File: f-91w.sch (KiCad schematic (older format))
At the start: 19 parts, among them P10 CONN_01X01, P11 CONN_01X01, P13 CONN_01X01, P14 CONN_01X01, P5 CONN_01X01, P6 CONN_01X01, P7 CONN_01X01, P8 CONN_01X01, P9 CONN_01X01, Q1 BC846, U2 LCD-F-91W, U3 TSOP57xxx, U4 MAG3110

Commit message: Add PSoC 4, decoupling and crystals
No connection to rest of system yet
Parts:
- added AE?: TBD, symbol Antenna_Shield
- added C?: 24pF, symbol C_Small
- added C?: 47pF, symbol C_Small
- added C? (x2): C_Small, symbol C_Small
- added C?: 1uF, symbol C_Small
- added L?: L_Small, symbol L_Small
- added U?: CY8C4248LQI-BL483, symbol CY8C4248LQI-BL483
- added Y?: 32.768KHz, symbol Crystal_Small
- added Y?: 24MHz, symbol Crystal_GND24
- P10, P11, P13, P14, P5, P6, P7, P8, P9: symbol CONN_01X01 -> Conn_01x01
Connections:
- net labels added: /XRES, SWCLK, SWDIO, VDDA, VDDD, VDDR
- wire segments 74 -> 122
- no-connect marks 0 -> 1

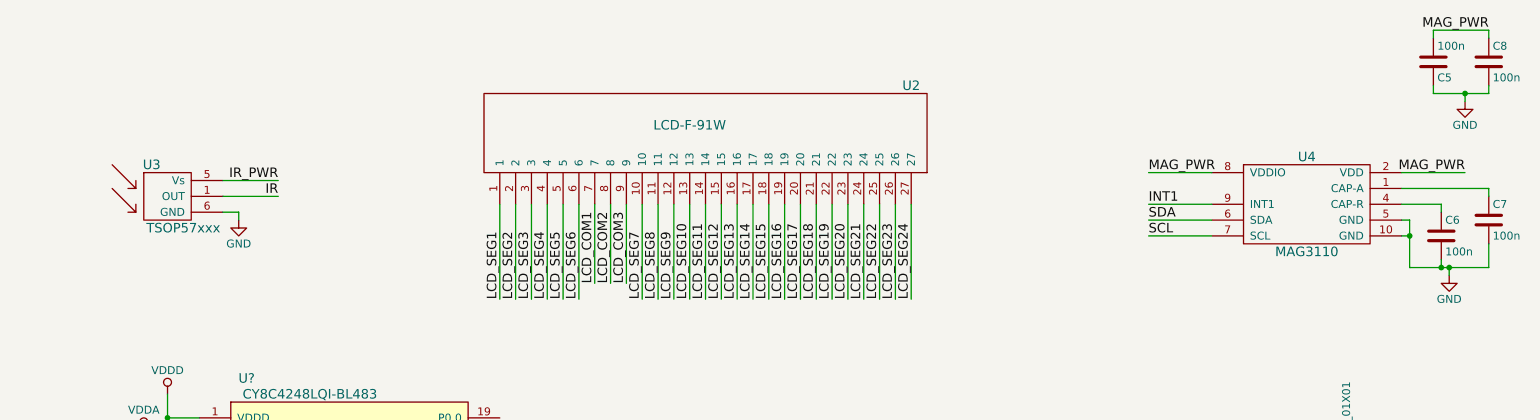
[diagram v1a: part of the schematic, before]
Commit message: Delete magnetometer and IR reciever
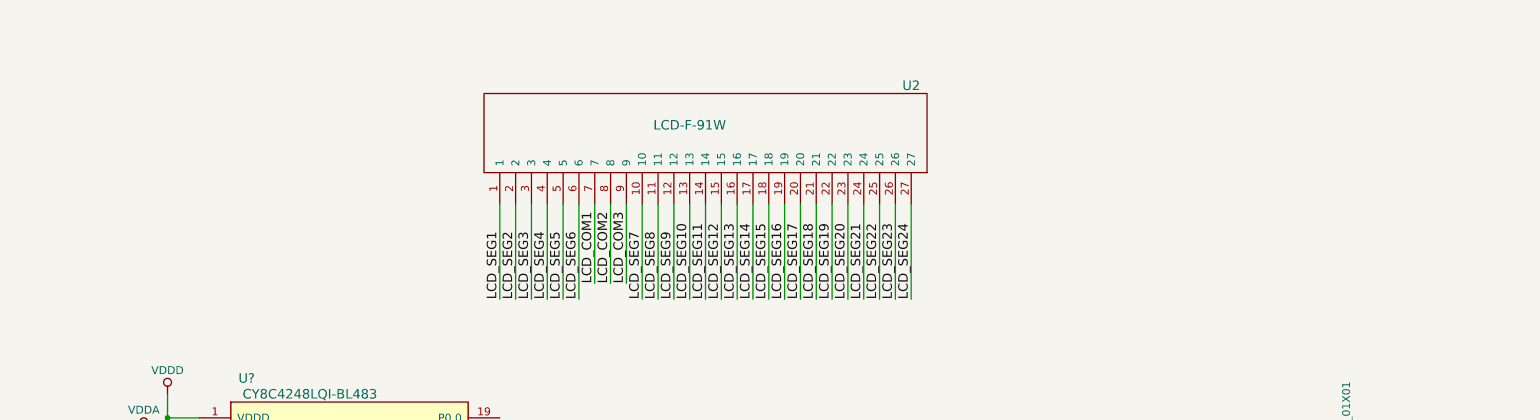
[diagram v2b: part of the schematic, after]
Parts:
- removed C5, C6, C7, C8: 100n, Capacitors_SMD:C_0402, symbol C
- removed U3: TSOP57xxx, f-91w:TSOP57xxx, symbol TSOP57xxx
- removed U4: MAG3110, Housings_DFN_QFN:DFN-10-1EP_2x2mm_Pitch0.4mm, symbol MAG3110
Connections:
- net labels removed: INT1, IR, IR_PWR, MAG_PWR, SCL, SDA
- wire segments 122 -> 95
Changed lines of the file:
@@
 $EndComp
-$Comp
-L TSOP57xxx U3
-U 1 1 56F47D47
-P 2350 1800
-F 0 "U3" H 2250 2000 60  0000 C CNN
-F 1 "TSOP57xxx" H 2450 1600 60  0000 C CNN
-F 2 "f-91w:TSOP57xxx" H 2350 1800 60  0001 C CNN
-F 3 "" H 2350 1800 60  0000 C CNN
-	1    2350 1800
-	1    0    0    -1
-$EndComp
-$Comp
-L GND #PWR02
-U 1 1 56F47FA1
-P 2800 1950
-F 0 "#PWR02" H 2800 1700 50  0001 C CNN
-F 1 "GND" H 2800 1800 50  0000 C CNN
-F 2 "" H 2800 1950 50  0000 C CNN
-F 3 "" H 2800 1950 50  0000 C CNN
-	1    2800 1950
-	1    0    0    -1
-$EndComp
-Text Label 3050 1700 2    60   ~ 0
-IR_PWR
-Text Label 3050 1800 2    60   ~ 0
-IR
 $Comp
 L R R3
@@
 	1    0    0    -1
 $EndComp
-$Comp
-L C C5
-U 1 1 5700E1C2
-P 10350 950
-F 0 "C5" H 10375 1050 50  0000 L CNN
-F 1 "100n" H 10375 850 50  0000 L CNN
-F 2 "Capacitors_SMD:C_0402" H 10388 800 50  0001 C CNN
-F 3 "" H 10350 950 50  0000 C CNN
-	1    10350 950
-	1    0    0    1
-$EndComp
-$Comp
-L GND #PWR06
-U 1 1 5700F75E
-P 10550 1200
-F 0 "#PWR06" H 10550 950 50  0001 C CNN
-F 1 "GND" H 10550 1050 50  0000 C CNN
-F 2 "" H 10550 1200 50  0000 C CNN
-F 3 "" H 10550 1200 50  0000 C CNN
-	1    10550 1200
-	1    0    0    -1
-$EndComp
-$Comp
-L GND #PWR07
-U 1 1 5700F854
-P 10450 2300
-F 0 "#PWR07" H 10450 2050 50  0001 C CNN
-F 1 "GND" H 10450 2150 50  0000 C CNN
-F 2 "" H 10450 2300 50  0000 C CNN
-F 3 "" H 10450 2300 50  0000 C CNN
-	1    10450 2300
-	1    0    0    -1
-$EndComp
-$Comp
-L C C6
-U 1 1 5700FED8
-P 10400 2050
-F 0 "C6" H 10425 2150 50  0000 L CNN
-F 1 "100n" H 10425 1950 50  0000 L CNN
-F 2 "Capacitors_SMD:C_0402" H 10438 1900 50  0001 C CNN
-F 3 "" H 10400 2050 50  0000 C CNN
-	1    10400 2050
-	1    0    0    -1
-$EndComp
-$Comp
-L C C7
-U 1 1 5700FF6D
-P 10700 1950
-F 0 "C7" H 10725 2050 50  0000 L CNN
-F 1 "100n" H 10725 1850 50  0000 L CNN
-F 2 "Capacitors_SMD:C_0402" H 10738 1800 50  0001 C CNN
-F 3 "" H 10700 1950 50  0000 C CNN
-	1    10700 1950
-	1    0    0    -1
-$EndComp
-Text Label 8550 1850 0    60   ~ 0
-INT1
-Text Label 8550 1950 0    60   ~ 0
-SDA
-Text Label 8550 2050 0    60   ~ 0
-SCL
-$Comp
-L MAG3110 U4
-U 1 1 57006D5B
-P 9550 1900
-F 0 "U4" H 9550 2250 60  0000 C CNN
-F 1 "MAG3110" H 9550 1650 60  0000 C CNN
-F 2 "Housings_DFN_QFN:DFN-10-1EP_2x2mm_Pitch0.4mm" H 9550 1900 60  0001 C CNN
-F 3 "" H 9550 1900 60  0000 C CNN
-	1    9550 1900
-	1    0    0    -1
-$EndComp
 Text Label 10100 3800 2    60   ~ 0
 BUZ
-$Comp
-L C C8
-U 1 1 57057DE2
-P 10700 950
-F 0 "C8" H 10725 1050 50  0000 L CNN
-F 1 "100n" H 10725 850 50  0000 L CNN
-F 2 "Capacitors_SMD:C_0402" H 10738 800 50  0001 C CNN
-F 3 "" H 10700 950 50  0000 C CNN
-	1    10700 950
-	1    0    0    -1
-$EndComp
 Text Label 8400 4350 2    60   ~ 0
 B_ALARM
@@
 Text Label 9400 4950 2    60   ~ 0
 LED_2
-Text Label 8550 1650 0    60   ~ 0
-MAG_PWR
-Text Label 10700 750  2    60   ~ 0
-MAG_PWR
-Text Label 10550 1650 2    60   ~ 0
-MAG_PWR
 $Comp
 L GND #PWR08
@@
 	8800 4050 9150 4050
 Wire Wire Line
-	2700 1700 3050 1700
-Wire Wire Line
-	2800 1950 2800 1900
-Wire Wire Line
-	2800 1900 2700 1900
-Wire Wire Line
-	2700 1800 3050 1800
-Wire Wire Line
 	10050 4700 9800 4700
 Wire Wire Line
 	7000 5050 7000 4900
 Wire Wire Line
-	8950 1650 8550 1650
-Wire Wire Line
 	6550 4600 6600 4600
 Wire Wire Line
@@
 	9400 4950 9750 4950
 Wire Wire Line
-	10350 1150 10350 1100
-Wire Wire Line
-	10150 1950 10200 1950
-Wire Wire Line
-	10200 1950 10200 2250
-Wire Wire Line
-	10150 2050 10200 2050
-Connection ~ 10200 2050
-Wire Wire Line
-	10150 1750 10700 1750
-Wire Wire Line
-	10700 1750 10700 1800
-Wire Wire Line
-	10150 1850 10400 1850
-Wire Wire Line
-	10400 1850 10400 1900
-Wire Wire Line
-	10200 2250 10700 2250
-Wire Wire Line
-	10700 2250 10700 2100
-Wire Wire Line
-	10400 2200 10400 2250
-Connection ~ 10400 2250
-Wire Wire Line
-	10450 2250 10450 2300
-Connection ~ 10450 2250
-Wire Wire Line
-	8550 1950 8950 1950
-Wire Wire Line
-	8550 2050 8950 2050
-Wire Wire Line
-	8950 1850 8550 1850
-Wire Wire Line
 	7950 4350 8600 4350
-Wire Wire Line
-	10350 800  10350 750
-Wire Wire Line
-	10150 1650 10550 1650
 Wire Wire Line
 	6550 4550 6550 4600
@@
 Connection ~ 9800 3800
 Wire Wire Line
-	10700 750  10700 800
-Wire Wire Line
-	10350 1150 10700 1150
-Wire Wire Line
-	10700 1150 10700 1100
-Wire Wire Line
-	10550 1200 10550 1150
-Connection ~ 10550 1150
-Wire Wire Line
-	10350 750  10700 750
-Wire Wire Line
 	2550 6950 2450 6950

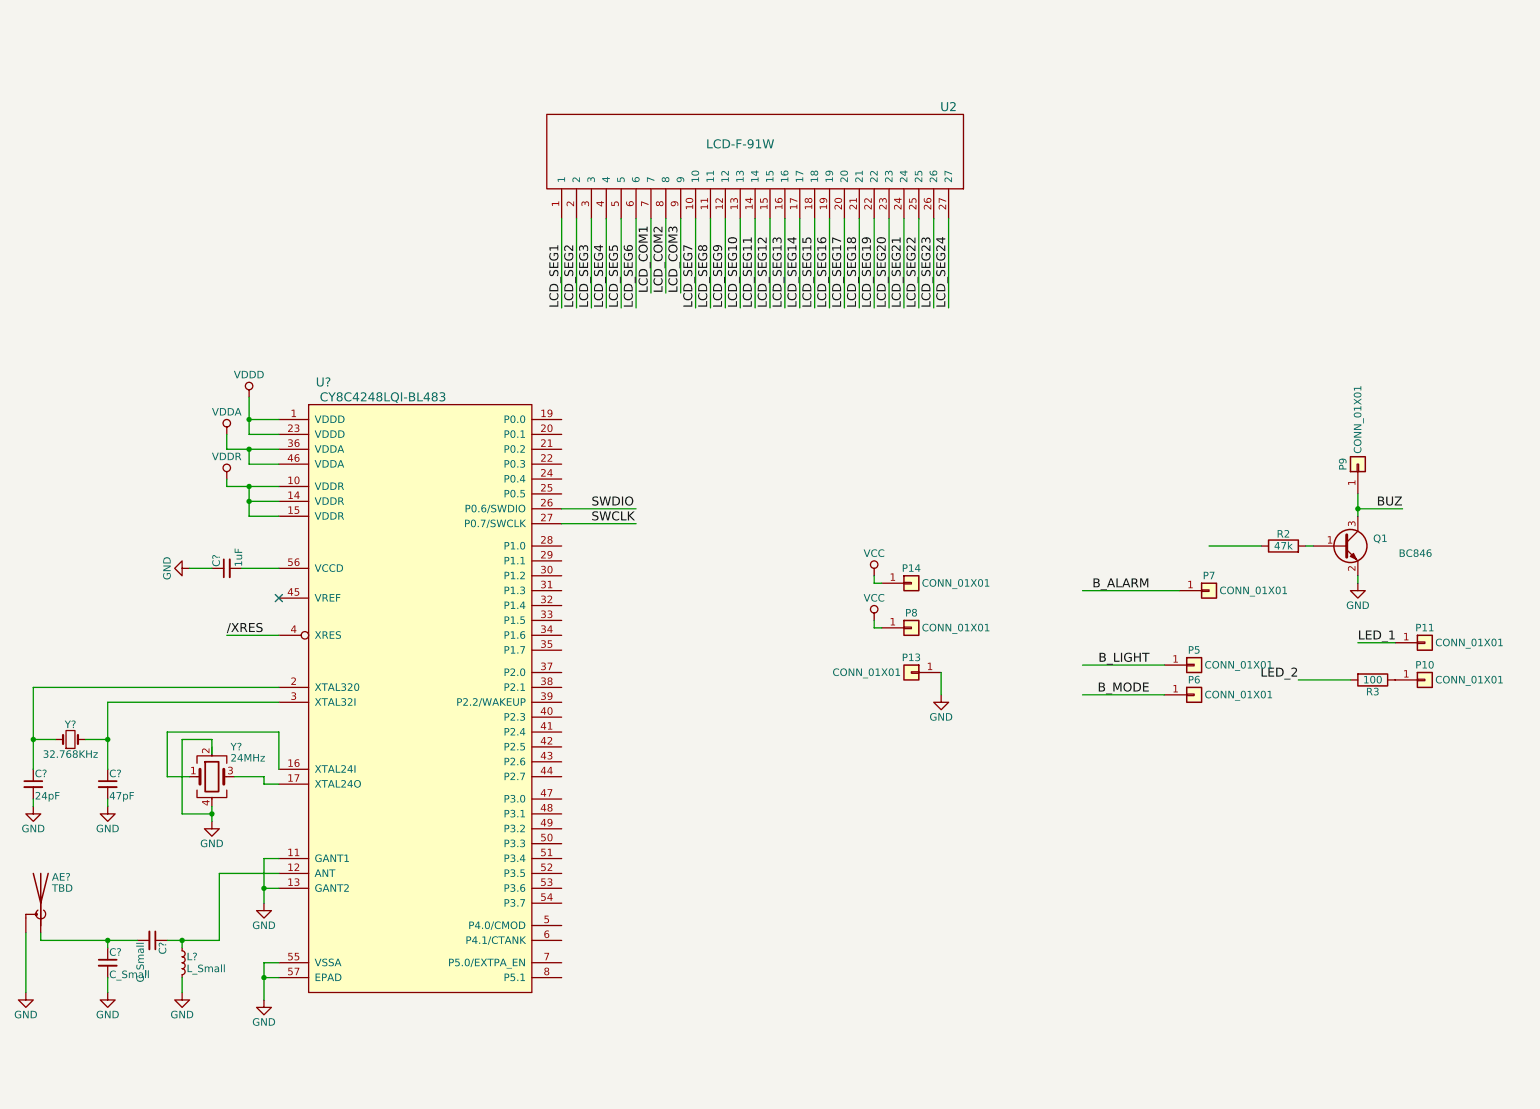
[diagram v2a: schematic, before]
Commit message: Add BME680 to schematic
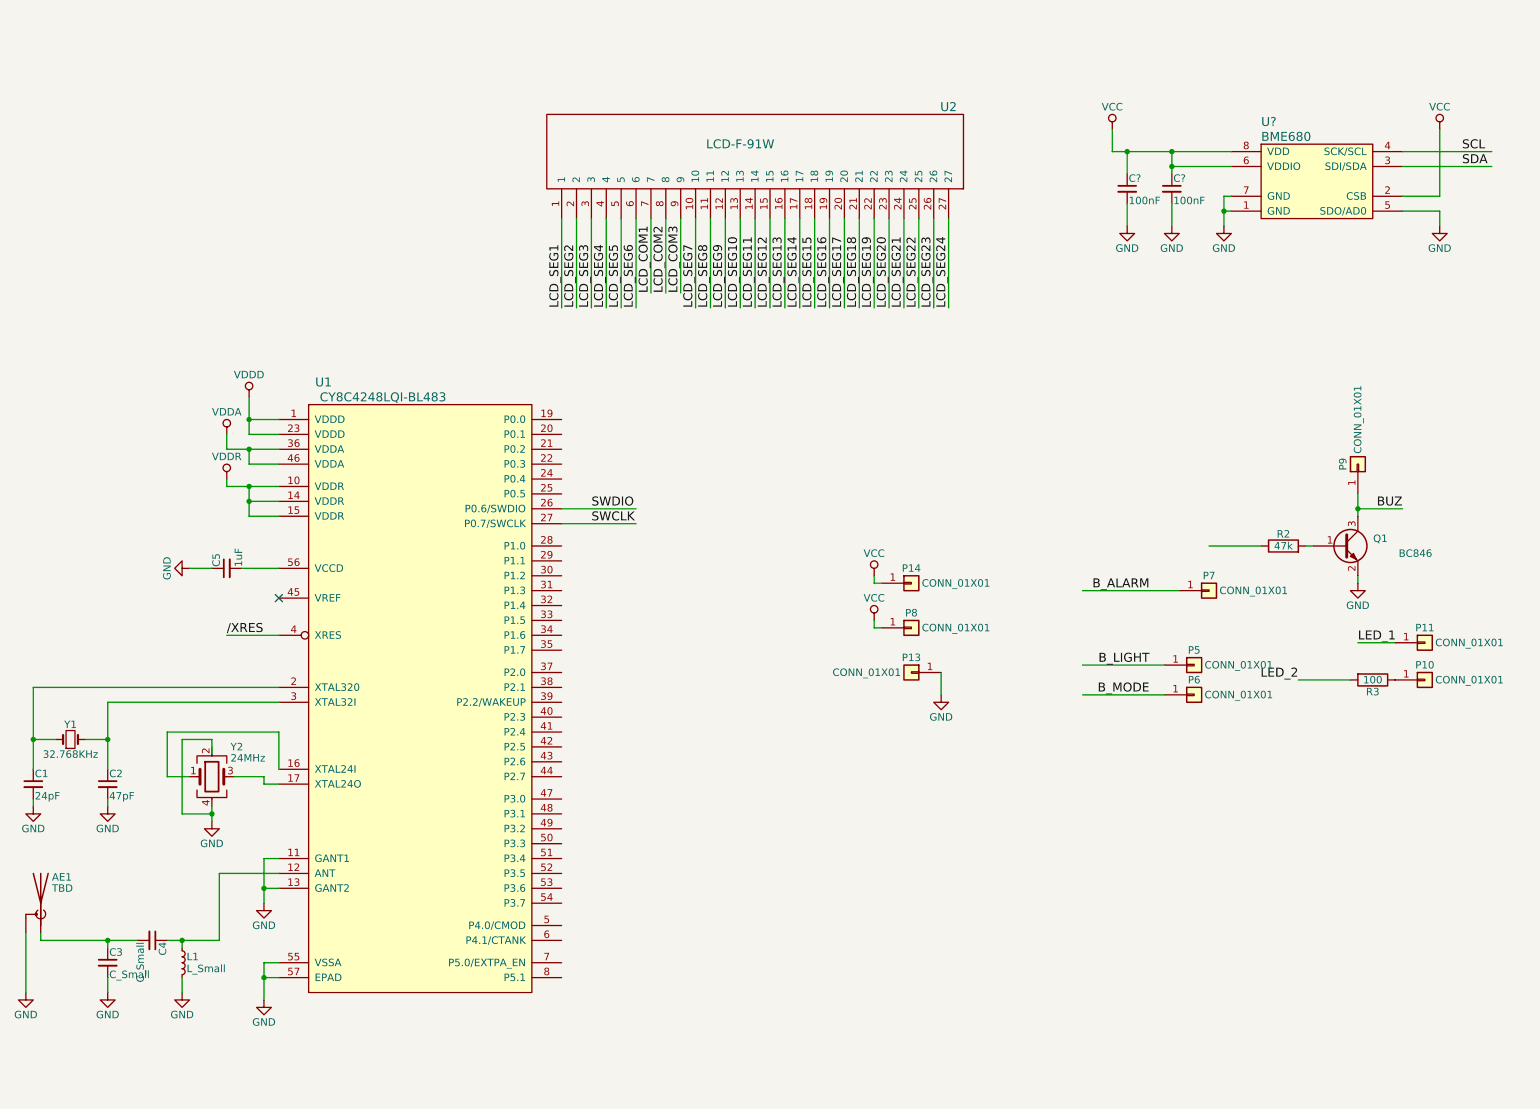
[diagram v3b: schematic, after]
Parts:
- added C? (x2): 100nF, symbol C_Small
- added U?: BME680, symbol BME680
- gave numbers to parts that had none: 10
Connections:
- net labels added: SCL, SDA
- wire segments 95 -> 127

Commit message: Add power and decoupling for PSOC
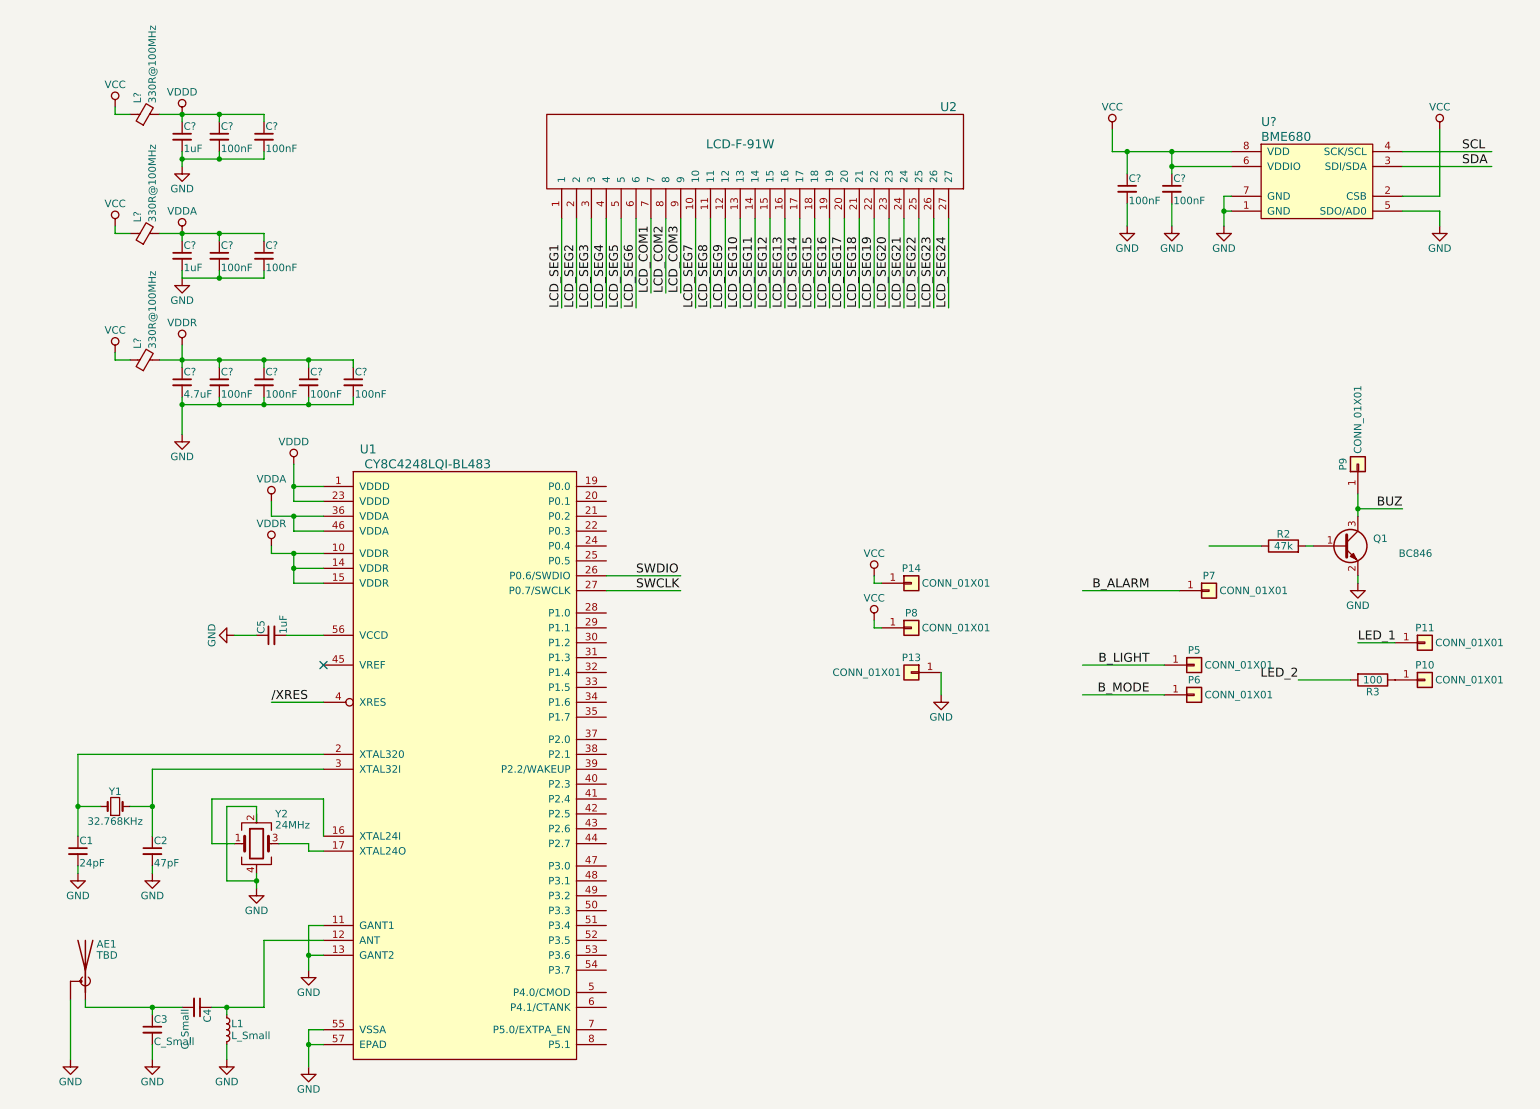
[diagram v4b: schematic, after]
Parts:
- added C?: 4.7uF, Capacitors_SMD:C_0402, symbol C_Small
- added C? (x8): 100nF, Capacitors_SMD:C_0201_NoSilk, symbol C_Small
- added C? (x2): 1uF, Capacitors_SMD:C_0201_NoSilk, symbol C_Small
- added L? (x3): 330R@100MHz, Resistors_SMD:R_0201_NoSilk, symbol Ferrite_Bead_Small
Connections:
- wire segments 127 -> 145
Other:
- moved on the sheet: AE1, C1, C2, C3, C4, C5, L1, U1, Y1, Y2
